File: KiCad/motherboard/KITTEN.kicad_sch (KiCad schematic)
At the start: 40 parts, among them J1 Barrel_Jack_Switch, J10 Conn_01x02_Pin, J2 Conn_01x03_Pin, J3 Conn_01x04_Pin, J4 Conn_01x05_Pin, J5 Conn_01x06_Pin, J6 Conn_01x07_Pin, J7 Conn_01x08_Pin, J8 Conn_01x09_Pin, J9 Conn_01x10_Pin, SW1 Cherry Switch Single, SW10 Cherry Switch Single, SW11 Cherry Switch Single, SW12 Cherry Switch Single, SW13 Cherry Switch Single, SW2 Cherry Switch 1.5x - Enter Key, SW3 Cherry Switch Single, SW4 Cherry Switch Single, SW5 Cherry Switch Single, SW6 Cherry Switch Single, SW7 Cherry Switch Single, SW9 Cherry Switch Single, U2 TMC2209, U3 Display, U4 ICM-20948, U5 24LC512, U6 Adafruit_ICM20948, U7 LTV-817S

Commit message: Work on schematics
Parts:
- removed R1, R10, R11, R2, R3, R4, R5, R6, R7, R8, R9: R, Resistor_SMD:R_0603_1608Metric, symbol Device:R
- removed SW10, SW11, SW12, SW13, SW3, SW4, SW5, SW6, SW7, SW9: Cherry Switch Single, ComponentLib:SW_Cherry_MX_1.00u_PCB, symbol Switch:SW_Push
- removed U4: ICM-20948, ComponentLib:ICM-20948, symbol Sensor_Motion:ICM-20948
- removed U6: Adafruit_ICM20948, ComponentLib:Adafruit-ICM-20948, symbol SymbolLib:Adafruit_ICM20948
- added J11, J12: Conn_01x06_Pin, Connector_JST:JST_PH_B6B-PH-K_1x06_P2.00mm_Vertical, symbol Connector:Conn_01x06_Pin
- added J13: Conn_01x04_Pin, Connector_JST:JST_PH_B4B-PH-K_1x04_P2.00mm_Vertical, symbol Connector:Conn_01x04_Pin
- added U8: TMC2209, ComponentLib:TMC2209 Silentstepstick, symbol SymbolLib:TMC2209_Silentstepstick
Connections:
- net GND: now also J3.4 (Pin_4), J4.4 (Pin_4), J11.2 (Pin_2), J12.2 (Pin_2)
- net +5V: now reaches J3.1 (Pin_1)
- net VREF_measback: now reaches J3.2 (Pin_2)
- net NumpadOut_toADC: now reaches J3.3 (Pin_3)
- net SCL: now reaches J4.1 (Pin_1)
- net SDA: now reaches J4.2 (Pin_2)
- net +3V3: now reaches J4.3 (Pin_3)
- net +3V3: now also J11.1 (Pin_1), J12.1 (Pin_1)
- net ~{RES}: now reaches J4.5 (Pin_5)
- new net CLK: J11.4 (Pin_4), J12.4 (Pin_4)
- new net CS_ENCODER1: J11.3 (Pin_3)
- new net CS_ENCODER2: J12.3 (Pin_3)
- new net MISO: J11.6 (Pin_6), J12.6 (Pin_6)
- new net MOSI: J11.5 (Pin_5), J12.5 (Pin_5)
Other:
- note added: "ICM20948"
- moved on the sheet: J3, J4, U2

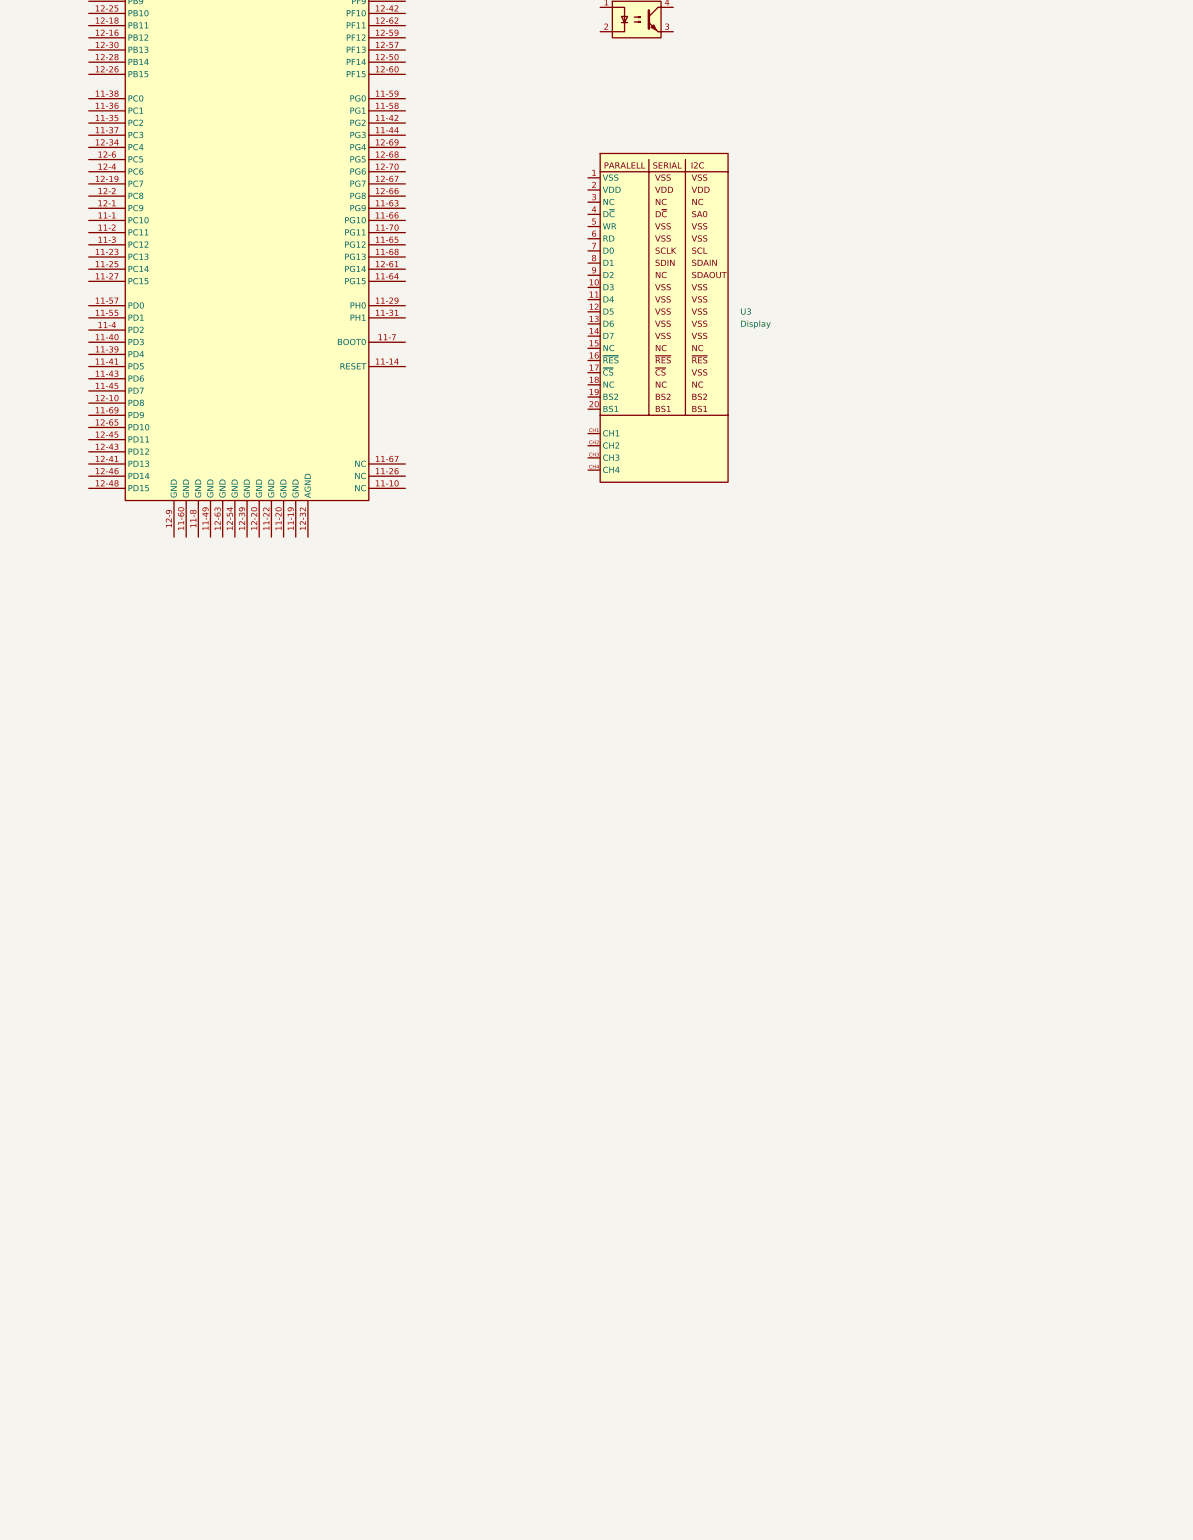
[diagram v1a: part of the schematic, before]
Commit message: Buttons module and main board schematics
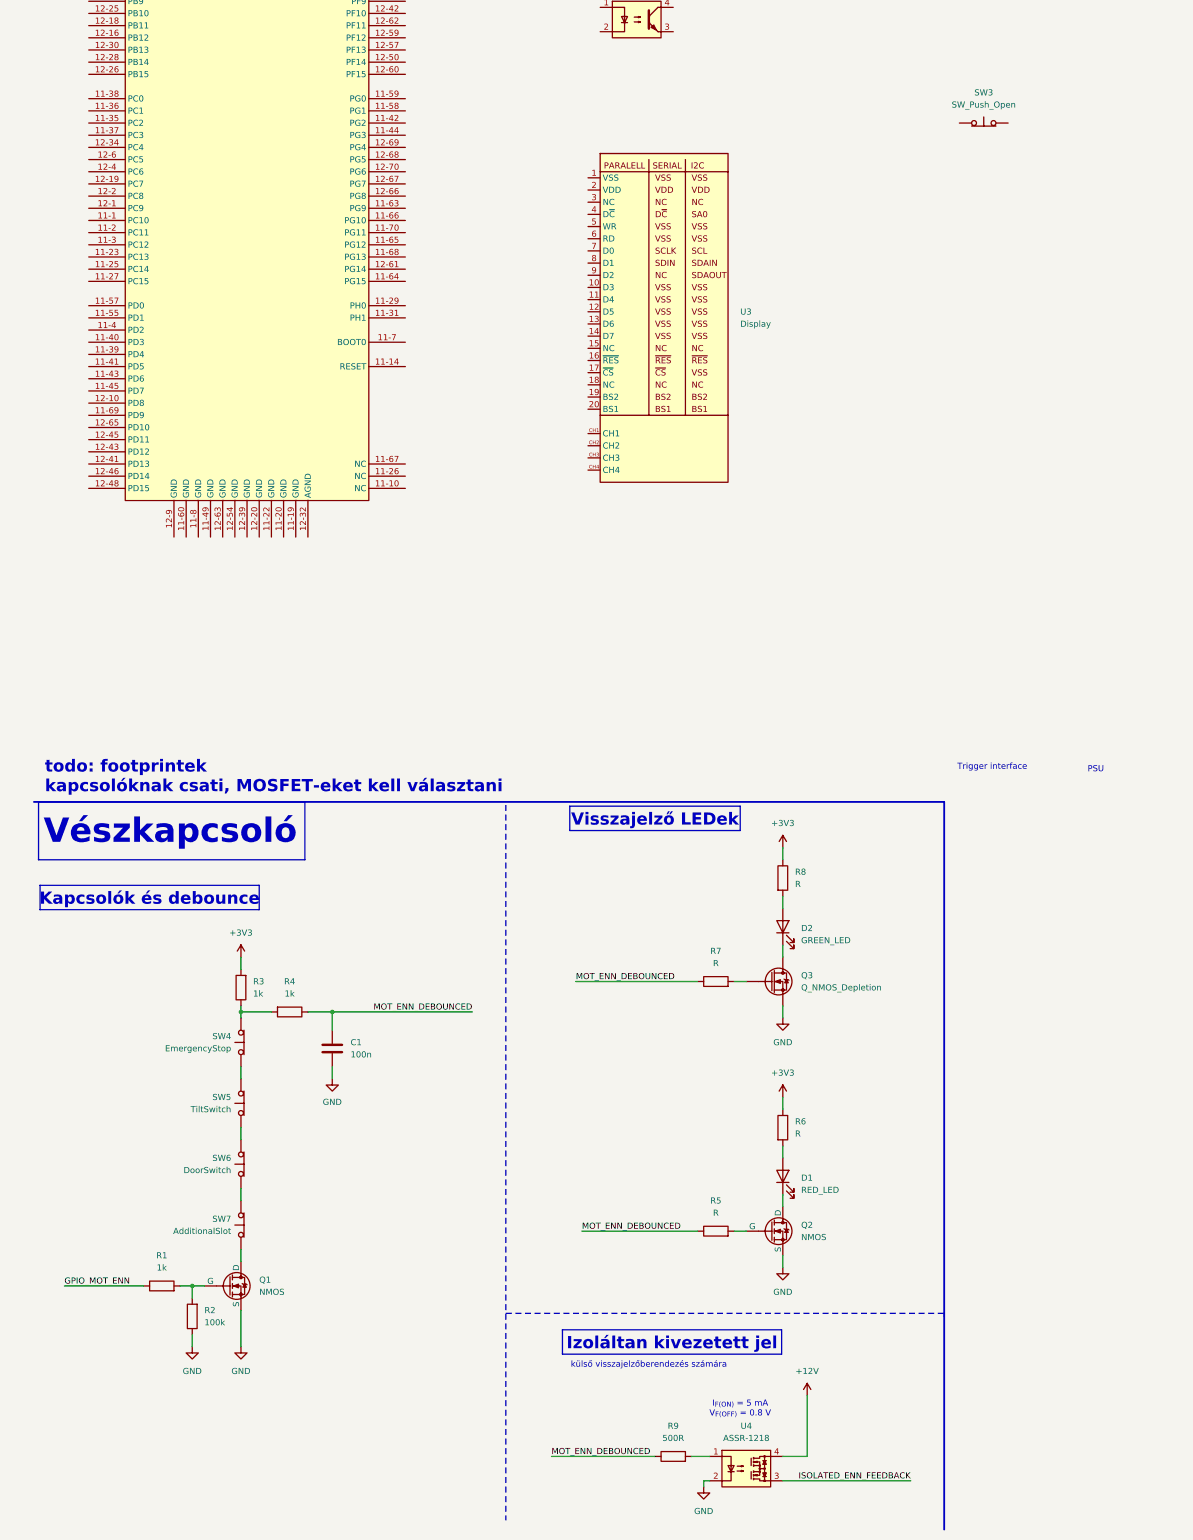
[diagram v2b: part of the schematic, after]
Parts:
- added C1: 100n, symbol Device:C
- added D1: RED_LED, symbol Device:LED
- added D2: GREEN_LED, symbol Device:LED
- added Q1, Q2: NMOS, symbol Simulation_SPICE:NMOS
- added Q3: Q_NMOS_Depletion, symbol Device:Q_NMOS_Depletion
- added R1, R3, R4: 1k, symbol Device:R
- added R2: 100k, symbol Device:R
- added R5, R6, R7, R8: R, symbol Device:R
- added R9: 500R, symbol Device:R
- added SW3: SW_Push_Open, symbol Switch:SW_Push_Open
- added SW4: EmergencyStop, symbol Switch:SW_Push_Open
- added SW5: TiltSwitch, symbol Switch:SW_Push_Open
- added SW6: DoorSwitch, symbol Switch:SW_Push_Open
- added SW7: AdditionalSlot, symbol Switch:SW_Push_Open
- added U4: ASSR-1218, Package_SO:SO-4_4.4x4.3mm_P2.54mm, symbol Relay_SolidState:ASSR-1218
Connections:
- net +3V3: now also R3.2, R6.1, R8.1
- net GND: now also C1.2, Q1.3 (S), Q2.3 (S), Q3.S, R2.1, U4.2
- new net: Q1.2 (G), R1.2, R2.2
- new net: D1.2 (A), R6.2
- new net: D2.1 (K), Q3.D
- new net: D2.2 (A), R8.2
- new net: D1.1 (K), Q2.1 (D)
- new net: Q1.1 (D), SW7.1 (A)
- new net: R3.1, R4.2, SW4.2 (B)
- new net: Q3.G, R7.2
- new net: Q2.2 (G), R5.2
- new net: R9.2, U4.1
- new net: SW6.1 (A), SW7.2 (B)
- new net: SW5.1 (A), SW6.2 (B)
- new net: SW4.1 (A), SW5.2 (B)
- new net +12V: U4.4
- new net GPIO_MOT_ENN: R1.1
- new net ISOLATED_ENN_FEEDBACK: U4.3
- new net MOT_ENN_DEBOUNCED: C1.1, R4.1, R5.1, R7.1, R9.1
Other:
- note added: "I_{F(ON)} = 5 mA V_{F(OFF)} = 0.8 V"
- note added: "Izoláltan kivezetett jel"
- note added: "Kapcsolók és debounce"
- note added: "PSU"
- note added: "Trigger interface"
- note added: "Visszajelző LEDek"
- note added: "Vészkapcsoló"
- note added: "külső visszajelzőberendezés számára"
- note added: "todo: footprintek kapcsolóknak csati, MOSFET-eket kell választani"

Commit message: Main sch further development
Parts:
- removed U3: Display, ComponentLib:NHD-2.23-12832UCB3, symbol SymbolLib:NHD-2.23-12832UCB3
- removed U8: TMC2209, ComponentLib:TMC2209 Silentstepstick, symbol SymbolLib:TMC2209_Silentstepstick
- added C14, C15, C16, C17, C6, C7, C9: 1u, symbol Device:C
- added C18, C19, C20, C21: 100n, Capacitor_SMD:C_0603_1608Metric, symbol Device:C
- added C2, C3, C4, C5: 22u, 35V, symbol Device:C
- added C8: 100n, symbol Device:C
- added D10, D11, D4, D6, D7, D8, D9: GREEN_LED, symbol Device:LED
- added D3: SM15T36CA, Diode_SMD:ST_D_SMC, symbol Diode:SM15T36CA
- added D5: RED_LED, symbol Device:LED
- added F1: Fuse, symbol Device:Fuse
- added J14, J15: Conn_01x04_Pin, Connector_JST:JST_PH_B4B-PH-K_1x04_P2.00mm_Vertical, symbol Connector:Conn_01x04_Pin
- added J16: Conn_01x05_Socket, symbol Connector:Conn_01x05_Socket
- added J17: DB25_Socket_MountingHoles, Connector_Dsub:DSUB-25_Socket_Horizontal_P2.77x2.84mm_EdgePinOffset7.70mm_Housed_MountingHolesOffset9.12mm, symbol Connector:DB25_Socket_MountingHoles
- added J18: Conn_01x09_Pin, Connector_JST:JST_PH_B9B-PH-K_1x09_P2.00mm_Vertical, symbol Connector:Conn_01x09_Pin
- added JP10, JP100, JP101, JP102, JP103, JP104, JP105, JP106, JP107, JP108, JP109, JP11, JP110, JP111, JP112, JP113, JP114, JP115, JP116, JP117, JP118, JP12, JP13, JP14, JP15, JP16, JP17, JP18, JP19, JP20, JP21, JP22, JP23, JP24, JP25, JP26, JP27, JP28, JP29, JP30, JP31, JP32, JP33, JP34, JP35, JP36, JP37, JP38, JP39, JP40, JP41, JP42, JP43, JP44, JP45, JP46, JP47, JP48, JP49, JP50, JP51, JP52, JP53, JP54, JP55, JP56, JP57, JP58, JP59, JP6, JP60, JP61, JP62, JP63, JP64, JP65, JP66, JP67, JP68, JP69, JP7, JP70, JP71, JP72, JP73, JP74, JP75, JP76, JP77, JP78, JP79, JP8, JP80, JP81, JP82, JP83, JP84, JP85, JP86, JP87, JP88, JP89, JP9, JP90, JP91, JP92, JP93, JP94, JP95, JP96, JP97, JP98, JP99: SolderJumper_2_Open, Resistor_SMD:R_0603_1608Metric_Pad0.98x0.95mm_HandSolder, symbol Jumper:SolderJumper_2_Open
- added JP2, JP3, JP4: SolderJumper_2_Open, symbol Jumper:SolderJumper_2_Open
- added Q10, Q5, Q6, Q7, Q8, Q9: BSS138, Package_TO_SOT_SMD:SOT-23, symbol Transistor_FET:BSS138
- added Q4: Si2371EDS, Package_TO_SOT_SMD:SOT-23, symbol Transistor_FET:Si2371EDS
- added R10, R11, R12, R13: R, symbol Device:R
- added R14, R15, R16, R17, R20, R22, R24, R40, R43, R45, R48, R50, R53, R55, R58: 1k, symbol Device:R
- added R18, R21, R27, R28, R29, R30, R42, R47, R52, R57: 100k, symbol Device:R
- added R19, R23, R41, R46, R51, R56: 190R, symbol Device:R
- added R25, R26, R39, R44, R49, R54: 100R, symbol Device:R
- added R59, R61, R63, R65: 1k, Resistor_SMD:R_0603_1608Metric, symbol Device:R
- added R60, R62, R64, R66: 10k, Resistor_SMD:R_0603_1608Metric, symbol Device:R
- added SW12: SW_Push, Connector_PinSocket_2.54mm:PinSocket_1x02_P2.54mm_Vertical, symbol Switch:SW_Push
- added SW13, SW14, SW15: SW_Push, symbol Switch:SW_Push
- added TP1, TP2, TP3, TP4, TP5, TP6: TestPoint, TestPoint:TestPoint_Pad_D2.0mm, symbol Connector:TestPoint
- added TP10, TP11, TP12, TP239, TP240, TP7, TP8, TP9: TestPoint, Connector_PinSocket_2.54mm:PinSocket_1x02_P2.54mm_Vertical, symbol Connector:TestPoint
- added TP100, TP101, TP102, TP103, TP104, TP105, TP106, TP107, TP108, TP109, TP110, TP111, TP112, TP113, TP114, TP115, TP116, TP117, TP118, TP119, TP120, TP121, TP122, TP123, TP124, TP125, TP126, TP127, TP128, TP129, TP13, TP130, TP131, TP132, TP133, TP134, TP135, TP136, TP137, TP138, TP139, TP14, TP140, TP141, TP142, TP143, TP144, TP145, TP146, TP147, TP148, TP149, TP15, TP150, TP151, TP152, TP153, TP154, TP155, TP156, TP157, TP158, TP159, TP16, TP160, TP161, TP162, TP163, TP164, TP165, TP166, TP167, TP168, TP169, TP17, TP170, TP171, TP172, TP173, TP174, TP175, TP176, TP177, TP178, TP179, TP18, TP180, TP181, TP182, TP183, TP184, TP185, TP186, TP187, TP188, TP189, TP19, TP190, TP191, TP192, TP193, TP194, TP195, TP196, TP197, TP198, TP199, TP20, TP200, TP201, TP202, TP203, TP204, TP205, TP206, TP207, TP208, TP209, TP21, TP210, TP211, TP212, TP213, TP214, TP215, TP216, TP217, TP218, TP219, TP22, TP220, TP221, TP222, TP223, TP224, TP225, TP226, TP227, TP228, TP229, TP23, TP230, TP231, TP232, TP233, TP234, TP235, TP236, TP237, TP238, TP24, TP25, TP26, TP27, TP28, TP29, TP30, TP31, TP32, TP33, TP34, TP35, TP36, TP37, TP38, TP39, TP40, TP41, TP42, TP43, TP44, TP45, TP46, TP47, TP48, TP49, TP50, TP51, TP52, TP53, TP54, TP55, TP56, TP57, TP58, TP59, TP60, TP61, TP62, TP63, TP64, TP65, TP66, TP67, TP68, TP69, TP70, TP71, TP72, TP73, TP74, TP75, TP76, TP77, TP78, TP79, TP80, TP81, TP82, TP83, TP84, TP85, TP86, TP87, TP88, TP89, TP90, TP91, TP92, TP93, TP94, TP95, TP96, TP97, TP98, TP99: TestPoint_Small, Connector_PinSocket_2.54mm:PinSocket_1x02_P2.54mm_Vertical, symbol Connector:TestPoint_Small
- added unit 9 of U1
- added unit 6 of U1
- added unit 8 of U1
- added unit 2 of U1
- added unit 4 of U1
- added unit 5 of U1
- added unit 3 of U1
- added unit 7 of U1
- added U10, U11, U12, U13, U14, U8: LTV-817S, Package_DIP:SMDIP-4_W9.53mm, symbol Isolator:LTV-817S
- added U3: TMC2209, ComponentLib:TMC2209 Silentstepstick, symbol SymbolLib:TMC2209_Silentstepstick
- added U6: P7805B-1000, symbol SymbolLib:P78B-1000
- added U9: P7803B-1000, symbol SymbolLib:P78B-1000
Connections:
- net +12V is gone; now on net +5V: U4.4
- net +3V3: now also J13.3 (Pin_3), U2.10 (VIO(3.3-5V)), U5.8 (VCC), C5.1, C8.1, C9.1, D8.2 (A), J18.1 (Pin_1), R28.1, R29.1, R30.1, SW12.2, SW13.2, SW14.2, SW15.2, U10.4, U12.4, U13.4, U14.4, U3.10 (VIO(3.3-5V)), U8.4, U9.3 (VOUT)
- net +5V: now also C14.1, C15.1, C16.1, C17.1, C3.1, C7.1, D7.2 (A), JP118.2 (B), R23.2, R41.2, R46.2, R51.2, R56.2, TP238.1, U6.3 (VOUT)
- net GND: now also J1.2, J1.3, J13.4 (Pin_4), U2.15 (GND), U2.9 (GND), U5.4 (GND), C14.2, C15.2, C16.2, C17.2, C18.2, C19.2, C2.2, C20.2, C21.2, C3.2, C4.2, C5.2, C7.2, C8.2, C9.2, D3.2 (A2), J18.9 (Pin_9), JP2.2 (B), JP3.2 (B), JP4.2 (B), Q6.2 (S), R10.2, R12.2, R13.2, R14.2, R15.2, R21.1, R22.1, R27.2, R40.1, R45.1, R50.1, R55.1, R60.2, R62.2, R64.2, R66.2, U1.11-19 (GND), U1.11-20 (GND), U1.11-22 (GND), U1.11-49 (GND), U1.11-60 (GND), U1.11-8 (GND), U1.12-20 (GND), U1.12-32 (AGND), U1.12-39 (GND), U1.12-54 (GND), U1.12-63 (GND), U1.12-9 (GND), U3.15 (GND), U3.9 (GND), U6.2 (GND), U9.2 (GND)
- net MOT_ENN_DEBOUNCED: now also U2.8 (EN), U3.8 (EN)
- net SCL: now also J13.1 (Pin_1), U5.6 (SCL)
- net SDA: now also J13.2 (Pin_2), U5.5 (SDA)
- net at J1.1: now also F1.1
- net MOT1_DIR: now reaches U2.1 (Dir)
- net at U2.11 (1B): now also J14.1 (Pin_1)
- net at U2.12 (1A): now also J14.2 (Pin_2)
- net at U2.13 (2A): now also J14.3 (Pin_3)
- net at U2.14 (2B): now also J14.4 (Pin_4)
- net +24V: now reaches U2.16 (VM)
- net +24V: now also C2.1, C4.1, D6.2 (A), Q4.2 (S), R11.1, U3.16 (VM), U6.1 (VIN), U9.1 (VIN)
- net MOT1_STEP: now reaches U2.2 (Step)
- net PDN_UART_MOT1: now reaches U2.3 (PDN/UART)
- net PDN_UART_MOT1: now also U2.4 (PDN/UART)
- net MOT1_SPREAD: now reaches U2.5 (SPREAD)
- net MOT1_MS2: now reaches U2.6 (MS2)
- net MOT1_MS1: now reaches U2.7 (MS1)
- net at U5.1 (A0): now also JP2.1 (A), R28.2
- net at U5.2 (A1): now also JP4.1 (A), R30.2
- net at U5.3 (A2): now also JP3.1 (A), R29.2
- net at U5.7 (WP): now also R27.1
- net at U1.11-13 (PA13): now also JP19.1 (A), TP39.1
- net at U1.11-15 (PA14): now also JP20.1 (A), TP41.1
- net at U1.11-17 (PA15): now also JP21.1 (A), TP43.1
- net at U1.11-28 (PA0): now also JP6.1 (A), TP15.1
- net at U1.11-30 (PA1): now also JP7.1 (A), TP14.1
- net at U1.11-32 (PA4): now also JP10.1 (A), TP21.1
- net at U1.12-11 (PA5): now also JP11.1 (A), TP23.1
- net at U1.12-12 (PA12): now also JP18.1 (A), TP37.1
- net at U1.12-13 (PA6): now also JP12.1 (A), TP25.1
- net at U1.12-14 (PA11): now also JP17.1 (A), TP35.1
- net at U1.12-15 (PA7): now also JP13.1 (A), TP27.1
- net at U1.12-21 (PA9): now also JP15.1 (A), TP31.1
- net at U1.12-23 (PA8): now also JP14.1 (A), TP29.1
- net at U1.12-33 (PA10): now also JP16.1 (A), TP33.1
- net at U1.12-35 (PA2): now also JP8.1 (A), TP17.1
- net at U1.12-37 (PA3): now also JP9.1 (A), TP19.1
- new net: R41.1, U8.1
- new net: JP33.2 (B), TP72.1
- new net: JP46.2 (B), TP101.1
- new net: J15.1 (Pin_1), U3.11 (1B)
- new net: J15.2 (Pin_2), U3.12 (1A)
- new net: J15.3 (Pin_3), U3.13 (2A)
- new net: J15.4 (Pin_4), U3.14 (2B)
- new net: JP87.1 (A), TP174.1, U1.11-55 (PD1)
- new net: JP11.2 (B), TP24.1
- new net: JP31.1 (A), TP54.1, U1.12-5 (PB9)
- new net: JP52.1 (A), TP91.1, U1.12-51 (PE14)
- new net: JP52.2 (B), TP107.1
- new net: D11.2 (A), R25.1, U11.3
- new net: JP100.1 (A), TP187.1, U1.12-46 (PD14)
- new net: JP100.2 (B), TP203.1
- new net: JP81.1 (A), TP152.1, U1.11-2 (PC11)
- new net: JP24.1 (A), TP47.1, U1.12-22 (PB2)
- new net: JP24.2 (B), TP63.1
- new net: R51.1, U13.1
- new net: Q9.3 (D), U13.2
- new net: R49.1, R50.2, U13.3
- new net: JP34.1 (A), TP57.1, U1.12-16 (PB12)
- new net: JP72.1 (A), TP143.1, U1.11-35 (PC2)
- new net: D11.1 (K), R24.2
- new net: JP88.1 (A), TP175.1, U1.11-4 (PD2)
- new net: JP73.1 (A), TP144.1, U1.11-37 (PC3)
- new net: JP118.1 (A), TP237.1, U1.11-6 (E5V)
- new net: JP88.2 (B), TP191.1
- new net: JP97.2 (B), TP200.1
- new net: Q7.1 (G), R42.2, R43.1
- new net: JP70.2 (B), TP157.1
- new net: JP60.1 (A), TP115.1, U1.11-9 (PF6)
- new net: JP60.2 (B), TP131.1
- new net: JP80.2 (B), TP167.1
- new net: JP106.2 (B), TP225.1
- new net: JP74.2 (B), TP161.1
- new net: JP94.1 (A), TP181.1, U1.12-10 (PD8)
- new net: Q10.1 (G), R57.2, R58.1
- new net: Q10.3 (D), U14.2
- new net: JP90.1 (A), TP177.1, U1.11-39 (PD4)
- new net: D10.1 (K), R22.2
- new net: JP21.2 (B), TP44.1
- new net: JP85.1 (A), TP156.1, U1.11-27 (PC15)
- new net: JP115.1 (A), TP218.1, U1.11-68 (PG13)
- new net: JP8.2 (B), TP18.1
- new net: JP50.2 (B), TP105.1
- new net: JP103.1 (A), TP206.1, U1.11-58 (PG1)
- new net: JP105.1 (A), TP208.1, U1.11-44 (PG3)
- new net: JP105.2 (B), TP224.1
- new net: JP53.2 (B), TP108.1
- new net: JP113.2 (B), TP232.1
- new net: JP25.2 (B), TP64.1
- new net: JP48.2 (B), TP103.1
- new net: JP84.1 (A), TP155.1, U1.11-25 (PC14)
- new net: JP84.2 (B), TP171.1
- new net: JP92.1 (A), TP179.1, U1.11-43 (PD6)
- new net: JP38.2 (B), TP93.1
- new net: JP99.1 (A), TP186.1, U1.12-41 (PD13)
- new net: Q9.1 (G), R52.2, R53.1
- new net: JP63.2 (B), TP134.1
- new net: JP33.1 (A), TP56.1, U1.12-18 (PB11)
- new net: Q8.1 (G), R47.2, R48.1
- new net: JP61.1 (A), TP116.1, U1.11-11 (PF7)
- new net: JP47.1 (A), TP86.1, U1.12-52 (PE9)
- new net: JP10.2 (B), TP22.1
- new net: JP85.2 (B), TP172.1
- new net: JP39.2 (B), TP94.1
- new net: JP14.2 (B), TP30.1
- new net: JP61.2 (B), TP132.1
- new net: JP23.2 (B), TP62.1
- new net: JP109.1 (A), TP212.1, U1.12-67 (PG7)
- new net: JP109.2 (B), TP228.1
- new net: R59.1, SW12.1
- new net: JP51.2 (B), TP106.1
- new net: JP116.1 (A), TP219.1, U1.12-61 (PG14)
- new net: JP116.2 (B), TP235.1
- new net: JP56.1 (A), TP111.1, U1.11-52 (PF2)
- new net: JP15.2 (B), TP32.1
- new net: JP29.2 (B), TP68.1
- new net: JP25.1 (A), TP48.1, U1.12-31 (PB3)
- new net: JP36.1 (A), TP59.1, U1.12-28 (PB14)
- new net: JP36.2 (B), TP75.1
- new net: R46.1, U12.1
- new net: Q8.3 (D), U12.2
- new net: R44.1, R45.2, U12.3
- new net: JP35.2 (B), TP74.1
- new net: JP104.1 (A), TP207.1, U1.11-42 (PG2)
- new net: JP79.1 (A), TP150.1, U1.12-1 (PC9)
- new net: JP58.1 (A), TP113.1, U1.12-38 (PF4)
- new net: JP102.1 (A), TP205.1, U1.11-59 (PG0)
- new net: JP102.2 (B), TP221.1
- new net: JP67.1 (A), TP122.1, U1.12-57 (PF13)
- new net: JP67.2 (B), TP138.1
- new net: JP43.2 (B), TP98.1
- new net: JP106.1 (A), TP209.1, U1.12-69 (PG4)
- new net: JP104.2 (B), TP223.1
- new net: JP59.2 (B), TP130.1
- new net: JP55.1 (A), TP110.1, U1.11-51 (PF1)
- new net: JP54.1 (A), TP109.1, U1.11-53 (PF0)
- new net: JP62.1 (A), TP117.1, U1.11-54 (PF8)
- new net: JP63.1 (A), TP118.1, U1.11-56 (PF9)
- new net: JP59.1 (A), TP114.1, U1.12-36 (PF5)
- new net: JP64.1 (A), TP119.1, U1.12-42 (PF10)
- new net: JP68.1 (A), TP123.1, U1.12-50 (PF14)
- new net: JP57.1 (A), TP112.1, U1.12-58 (PF3)
- new net: JP66.1 (A), TP121.1, U1.12-59 (PF12)
- new net: JP69.1 (A), TP124.1, U1.12-60 (PF15)
- new net: JP65.1 (A), TP120.1, U1.12-62 (PF11)
- new net: JP93.2 (B), TP196.1
- new net: JP74.1 (A), TP145.1, U1.12-34 (PC4)
- new net: JP98.1 (A), TP185.1, U1.12-43 (PD12)
- new net: JP48.1 (A), TP87.1, U1.12-47 (PE10)
- new net: JP38.1 (A), TP77.1, U1.12-64 (PE0)
- new net: JP75.1 (A), TP146.1, U1.12-6 (PC5)
- new net: JP73.2 (B), TP160.1
- new net: Q7.3 (D), U8.2
- new net: R39.1, R40.2, U8.3
- new net: R19.1, U10.1
- new net: JP39.1 (A), TP78.1, U1.11-61 (PE1)
- new net: JP30.1 (A), TP53.1, U1.12-3 (PB8)
- new net: JP79.2 (B), TP166.1
- new net: JP94.2 (B), TP197.1
- new net: D3.1 (A1), D4.2 (A), D5.1 (K), F1.2, Q4.3 (D)
- new net: JP115.2 (B), TP234.1
- new net: JP96.1 (A), TP183.1, U1.12-65 (PD10)
- new net: D6.1 (K), R13.1
- new net: JP28.2 (B), TP67.1
- new net: JP114.1 (A), TP217.1, U1.11-65 (PG12)
- new net: JP103.2 (B), TP222.1
- new net: R63.1, SW14.1
- new net: JP51.1 (A), TP90.1, U1.12-55 (PE13)
- new net: JP87.2 (B), TP190.1
- new net: JP44.2 (B), TP99.1
- new net: JP16.2 (B), TP34.1
- new net: JP98.2 (B), TP201.1
- new net: Q5.1 (G), R17.1, R18.2
- new net: JP37.1 (A), TP60.1, U1.12-26 (PB15)
- new net: JP37.2 (B), TP76.1
- new net: JP62.2 (B), TP133.1
- new net: JP28.1 (A), TP51.1, U1.12-17 (PB6)
- new net: JP27.1 (A), TP50.1, U1.12-29 (PB5)
- new net: JP27.2 (B), TP66.1
- new net: JP31.2 (B), TP70.1
- new net: JP99.2 (B), TP202.1
- new net: D9.1 (K), R16.2
- new net: JP111.1 (A), TP214.1, U1.11-63 (PG9)
- new net: JP111.2 (B), TP230.1
- new net: JP55.2 (B), TP126.1
- new net: JP50.1 (A), TP89.1, U1.12-49 (PE12)
- new net: JP101.1 (A), TP188.1, U1.12-48 (PD15)
- new net: JP101.2 (B), TP204.1
- new net: JP108.1 (A), TP211.1, U1.12-70 (PG6)
- new net: JP108.2 (B), TP227.1
- new net: JP92.2 (B), TP195.1
- new net: JP80.1 (A), TP151.1, U1.11-1 (PC10)
- new net: JP29.1 (A), TP52.1, U1.11-21 (PB7)
- new net: JP22.1 (A), TP45.1, U1.11-34 (PB0)
- new net: JP23.1 (A), TP46.1, U1.12-24 (PB1)
- new net: JP32.1 (A), TP55.1, U1.12-25 (PB10)
- new net: JP26.1 (A), TP49.1, U1.12-27 (PB4)
- new net: JP35.1 (A), TP58.1, U1.12-30 (PB13)
- new net: JP86.1 (A), TP173.1, U1.11-57 (PD0)
- new net: JP86.2 (B), TP189.1
- new net: JP113.1 (A), TP216.1, U1.11-70 (PG11)
- new net: JP49.1 (A), TP88.1, U1.12-56 (PE11)
- new net: JP49.2 (B), TP104.1
- new net: JP32.2 (B), TP71.1
- new net: JP19.2 (B), TP40.1
- new net: JP78.1 (A), TP149.1, U1.12-2 (PC8)
- new net: JP69.2 (B), TP140.1
- new net: JP6.2 (B), TP13.1
- new net: JP42.1 (A), TP81.1, U1.11-48 (PE4)
- new net: JP20.2 (B), TP42.1
- new net: JP76.2 (B), TP163.1
- new net: JP90.2 (B), TP193.1
- new net: JP66.2 (B), TP137.1
- new net: JP89.1 (A), TP176.1, U1.11-40 (PD3)
- new net: JP91.1 (A), TP178.1, U1.11-41 (PD5)
- new net: JP93.1 (A), TP180.1, U1.11-45 (PD7)
- new net: JP95.1 (A), TP182.1, U1.11-69 (PD9)
- new net: JP97.1 (A), TP184.1, U1.12-45 (PD11)
- new net: JP91.2 (B), TP194.1
- new net: JP65.2 (B), TP136.1
- new net: JP64.2 (B), TP135.1
- new net: JP71.1 (A), TP142.1, U1.11-36 (PC1)
- new net: JP40.1 (A), TP79.1, U1.11-46 (PE2)
- new net: JP41.1 (A), TP80.1, U1.11-47 (PE3)
- new net: JP43.1 (A), TP82.1, U1.11-50 (PE5)
- new net: JP44.1 (A), TP83.1, U1.11-62 (PE6)
- new net: JP46.1 (A), TP85.1, U1.12-40 (PE8)
- new net: JP45.1 (A), TP84.1, U1.12-44 (PE7)
- new net: JP53.1 (A), TP92.1, U1.12-53 (PE15)
- new net: R65.1, SW15.1
- new net: JP12.2 (B), TP26.1
- new net: Q6.1 (G), R20.1, R21.2
- new net: Q6.3 (D), U11.2
- new net: JP112.2 (B), TP231.1
- new net: JP82.1 (A), TP153.1, U1.11-3 (PC12)
- new net: JP42.2 (B), TP97.1
- new net: JP75.2 (B), TP162.1
- new net: JP114.2 (B), TP233.1
- new net: JP70.1 (A), TP141.1, U1.11-38 (PC0)
- new net: JP96.2 (B), TP199.1
- new net: D10.2 (A), R26.2, U10.3
- new net: JP77.2 (B), TP164.1
- new net: JP57.2 (B), TP128.1
- new net: JP13.2 (B), TP28.1
- new net: JP78.2 (B), TP165.1
- new net: JP17.2 (B), TP36.1
- new net: JP76.1 (A), TP147.1, U1.12-4 (PC6)
- new net: JP45.2 (B), TP100.1
- new net: JP112.1 (A), TP215.1, U1.11-66 (PG10)
- new net: JP34.2 (B), TP73.1
- new net: JP22.2 (B), TP61.1
- new net: R23.1, U11.1
- new net: JP30.2 (B), TP69.1
- new net: JP83.1 (A), TP154.1, U1.11-23 (PC13)
- new net: JP83.2 (B), TP170.1
- new net: D8.1 (K), R15.1
- new net: JP40.2 (B), TP95.1
- new net: JP47.2 (B), TP102.1
- new net: JP77.1 (A), TP148.1, U1.12-19 (PC7)
- new net: JP56.2 (B), TP127.1
- new net: JP71.2 (B), TP158.1
- new net: JP81.2 (B), TP168.1
- new net: JP95.2 (B), TP198.1
- new net: JP89.2 (B), TP192.1
- new net: JP82.2 (B), TP169.1
- new net: JP54.2 (B), TP125.1
- new net: JP7.2 (B), TP16.1
- new net: JP117.1 (A), TP220.1, U1.11-64 (PG15)
- new net: JP117.2 (B), TP236.1
- new net: JP41.2 (B), TP96.1
- new net: JP107.2 (B), TP226.1
- new net: JP107.1 (A), TP210.1, U1.12-68 (PG5)
- new net: JP110.1 (A), TP213.1, U1.12-66 (PG8)
- new net: Q4.1 (G), R11.2, R12.1
- new net: JP68.2 (B), TP139.1
- new net: D4.1 (K), D5.2 (A), R10.1
- new net: JP9.2 (B), TP20.1
- new net: JP26.2 (B), TP65.1
- new net: R54.1, R55.2, U14.3
- new net: D7.1 (K), R14.1
- new net: JP18.2 (B), TP38.1
- new net: JP58.2 (B), TP129.1
- new net: R56.1, U14.1
- new net: Q5.3 (D), U10.2
- new net: JP72.2 (B), TP159.1
- new net: JP110.2 (B), TP229.1
- new net: R61.1, SW13.1
- new net BTN_ADDITIONAL: J18.8 (Pin_8)
- new net BTN_FIX_AX: J18.2 (Pin_2)
- new net BTN_FREE_MOOVE: J18.7 (Pin_7)
- new net BTN_MEMSLOT: J18.4 (Pin_4)
- new net BTN_OK: J18.5 (Pin_5)
- new net BTN_SET: J18.6 (Pin_6)
- new net BTN_TRACKED_AX: J18.3 (Pin_3)
- new net CLK_LISTEN: R49.2, TP11.1
- new net CLK_LISTEN_EXTERNAL: J16.3 (Pin_3), R53.2, TP12.1
- new net EXTRA_BTN_1: C18.1, R59.2, R60.1
- new net EXTRA_BTN_2: C19.1, R61.2, R62.1
- new net EXTRA_BTN_3: C20.1, R63.2, R64.1
- new net EXTRA_BTN_4: C21.1, R65.2, R66.1
- new net GND_SPI_LISTEN: J16.5 (Pin_5), Q10.2 (S), Q7.2 (S), Q8.2 (S), Q9.2 (S), R42.1, R47.1, R52.1, R57.1
- new net GND_TRG: C6.2, J17.0 (PAD), J17.24 (P24), J17.25 (P25), J17.5, Q5.2 (S), R16.1, R18.1, R24.1, TP6.1
- new net MISO_LISTEN: R44.2, TP9.1
- new net MISO_LISTEN_EXTERNAL: J16.2 (Pin_2), R48.2, TP7.1
- new net MOSI_LISTEN: R39.2, TP10.1
- new net MOSI_LISTEN_EXTERNAL: J16.1 (Pin_1), R43.2, TP8.1
- new net MOT2_DIR: U3.1 (Dir)
- new net MOT2_MS1: U3.7 (MS1)
- new net MOT2_MS2: U3.6 (MS2)
- new net MOT2_SPREAD: U3.5 (SPREAD)
- new net MOT2_STEP: U3.2 (Step)
- new net NSS_LISTEN: R54.2, TP239.1
- new net NSS_LISTEN_EXTERNAL: J16.4 (Pin_4), R58.2, TP240.1
- new net PDN_UART_MOT2: U3.3 (PDN/UART), U3.4 (PDN/UART)
- new net SIMU_TRG_RB: J17.1, R25.2, TP1.1
- new net SIMU_TRG_SIGNAL: J17.12, R17.2, TP4.1
- new net TRG_RB_SIGNAL: R20.2, TP2.1
- new net TRG_SIGNAL: R26.1, TP3.1
- new net VCC_TRG: C6.1, D9.2 (A), J17.18 (P18), R19.2, TP5.1, U11.4
- no-connect marks 0 -> 6
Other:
- note added: "100R miért? Csak, h ne közvetlenül menjen?"
- note added: "Csatlakozó"
- note added: "DC-DC 3V3"
- note added: "DC-DC 5V"
- note added: "EEPROM"
- note added: "ENCODER 1"
- note added: "ESD"
- note added: "Ez csak placeholder, meg kell beszélni a típusát még"
- note added: "Ez nem tudom, jó választás-e. Azért ez van itt, mert ez már bennt volt a könyvtárnam, kétiránú és VRM = 30.8V"
- note added: "Ez így miért nem jó, hogy nem 5V és 3v3 zener, hanem simán a 3v3-at kapcsolom"
- note added: "GOMBOK"
- note added: "I_{C max} = 30 ma"
- note added: "MCU"
- note added: "MODULOK"
- note added: "Minden lábnál így"
- note added: "Motorvezérlők"
- note added: "NUMPAD"
- note added: "OELD"
- note added: "Polarity indication"
- note added: "Polarity indication?"
- note added: "Pull downt azért raktam, mert le van választva -> nincs aktívan hajtva az alacsony szint Nem terheli ezn agyon a lehallgatottat? Milyen csati kellene?"
- note added: "REF SZENZOR"
- note added: "SIMU"
- note added: "SPI SNIFFER"
- note added: "Simulizer -> MCU trigger jel izoláció"
- note added: "Simulizer <- MCU trigger jel izoláció"
- note added: "TOVÁBBI GOMBOK ELŐKÉSZÍTÉSE"
- note added: "Táp"
- note added: "V_{F} = 1.2V I_{F} = 20mA"
- note removed: "ICM20948"
- note removed: "PSU"
- moved on the sheet: J1, J10, J11, J12, J13, J2, J3, J4, J5, J6, J7, J8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

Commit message: MAIN board schematic mostly done
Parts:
- removed J10: Conn_01x02_Pin, Connector_JST:JST_PH_B2B-PH-K_1x02_P2.00mm_Vertical, symbol Connector:Conn_01x02_Pin
- removed J2: Conn_01x03_Pin, Connector_JST:JST_PH_B3B-PH-K_1x03_P2.00mm_Vertical, symbol Connector:Conn_01x03_Pin
- removed J5: Conn_01x06_Pin, Connector_JST:JST_PH_B6B-PH-K_1x06_P2.00mm_Vertical, symbol Connector:Conn_01x06_Pin
- removed J6: Conn_01x07_Pin, Connector_JST:JST_PH_B7B-PH-K_1x07_P2.00mm_Vertical, symbol Connector:Conn_01x07_Pin
- removed J7: Conn_01x08_Pin, Connector_JST:JST_PH_B8B-PH-K_1x08_P2.00mm_Vertical, symbol Connector:Conn_01x08_Pin
- removed J8: Conn_01x09_Pin, Connector_JST:JST_PH_B9B-PH-K_1x09_P2.00mm_Vertical, symbol Connector:Conn_01x09_Pin
- removed J9: Conn_01x10_Pin, Connector_JST:JST_PH_B10B-PH-K_1x10_P2.00mm_Vertical, symbol Connector:Conn_01x10_Pin
- removed SW1: Cherry Switch Single, ComponentLib:SW_Cherry_MX_1.00u_PCB, symbol Switch:SW_Push
- removed SW2: Cherry Switch 1.5x - Enter Key, ComponentLib:SW_Cherry_MX_1.50u_PCB, symbol Switch:SW_Push
- removed SW3: SW_Push_Open, symbol Switch:SW_Push_Open
- removed U7: LTV-817S, Package_DIP:SMDIP-4_W9.53mm, symbol Isolator:LTV-817S
- added R31, R32: R, symbol Device:R
- added TP241, TP242: TestPoint, Connector_PinSocket_2.54mm:PinSocket_1x02_P2.54mm_Vertical, symbol Connector:TestPoint
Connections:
- net BTN_ADDITIONAL is gone; now on net BTN_EXTERNAL_EXTRA: J18.8 (Pin_8)
- net CLK is gone; now on net SPI_SCK: J11.4 (Pin_4), J12.4 (Pin_4)
- net EXTRA_BTN_1 is gone; now on net BTN_ONBRD_EXTRA1: C18.1, R59.2, R60.1
- net EXTRA_BTN_2 is gone; now on net BTN_ONBRD_EXTRA2: C19.1, R61.2, R62.1
- net EXTRA_BTN_3 is gone; now on net BTN_ONBRD_EXTRA3: C20.1, R63.2, R64.1
- net EXTRA_BTN_4 is gone; now on net BTN_ONBRD_EXTRA4: C21.1, R65.2, R66.1
- net MISO is gone; now on net SPI_MISO: J11.6 (Pin_6), J12.6 (Pin_6)
- net MOSI is gone; now on net SPI_MOSI: J11.5 (Pin_5), J12.5 (Pin_5)
- net NumpadOut_toADC is gone; now on net NUMPAD_A_OUT: J3.3 (Pin_3)
- net SCL is gone; now on net I2C_SCL: J13.1 (Pin_1), J4.1 (Pin_1), U5.6 (SCL)
- net SDA is gone; now on net I2C_SDA: J13.2 (Pin_2), J4.2 (Pin_2), U5.5 (SDA)
- net TRG_RB_SIGNAL is gone; now on net TRG_RB_OUT: R20.2, TP2.1
- net VREF_measback is gone; now on net NUMPAD_VREF: J3.2 (Pin_2)
- net ~{RES} is gone; now on net OLED_~{RES}: J4.5 (Pin_5)
- net +3V3: now also R31.1, R32.1
- net BTN_FIX_AX: now also JP40.2 (B), TP95.1
- net BTN_FREE_MOOVE: now also JP45.2 (B), TP100.1
- net BTN_MEMSLOT: now also JP42.2 (B), TP97.1
- net BTN_OK: now also JP43.2 (B), TP98.1
- net BTN_SET: now also JP44.2 (B), TP99.1
- net BTN_TRACKED_AX: now also JP41.2 (B), TP96.1
- net CLK_LISTEN: now also JP32.2 (B), JP80.2 (B), TP167.1, TP71.1
- net CS_ENCODER1: now also JP64.2 (B), TP135.1
- net CS_ENCODER2: now also JP65.2 (B), TP136.1
- net GPIO_MOT_ENN: now also JP62.2 (B), TP133.1
- net MISO_LISTEN: now also JP24.2 (B), TP63.1
- net MOSI_LISTEN: now also JP73.2 (B), TP160.1
- net MOT1_DIR: now also JP54.2 (B), TP125.1
- net MOT1_MS1: now also JP56.2 (B), TP127.1
- net MOT1_MS2: now also JP57.2 (B), TP128.1
- net MOT1_SPREAD: now also JP55.2 (B), TP126.1
- net MOT1_STEP: now also JP6.2 (B), TP13.1
- net MOT2_DIR: now also JP58.2 (B), TP129.1
- net MOT2_MS1: now also JP60.2 (B), TP131.1
- net MOT2_MS2: now also JP61.2 (B), TP132.1
- net MOT2_SPREAD: now also JP59.2 (B), TP130.1
- net MOT2_STEP: now also JP21.2 (B), TP44.1
- net MOT_ENN_DEBOUNCED: now also JP38.2 (B), TP93.1
- net NSS_LISTEN: now also JP10.2 (B), JP34.2 (B), TP22.1, TP73.1
- net PDN_UART_MOT1: now also JP82.2 (B), TP169.1
- net PDN_UART_MOT2: now also JP87.2 (B), TP190.1
- net TRG_SIGNAL: now also JP39.2 (B), TP94.1
- net BTN_EXTERNAL_EXTRA: now reaches JP46.2 (B), TP101.1
- net MOT2_DIAG: now reaches U3.17 (DIAG)
- net MOT2_DIAG: now also JP52.2 (B), TP107.1
- net MOT2_INDEX: now reaches U3.18 (INDEX)
- net MOT2_INDEX: now also TP241.1
- net SPI_SCK: now reaches JP11.2 (B), TP24.1
- net BTN_ONBRD_EXTRA4: now reaches JP50.2 (B), TP105.1
- net BTN_ONBRD_EXTRA2: now reaches JP48.2 (B), TP103.1
- net OLED_~{RES}: now reaches JP63.2 (B), TP134.1
- net MOT1_DIAG: now reaches JP51.2 (B), TP106.1
- net MOT1_DIAG: now also U2.17 (DIAG)
- net SPI_MOSI: now reaches JP27.2 (B), TP66.1
- net I2C_SDA: now reaches JP31.2 (B), TP70.1
- net I2C_SDA: now also R32.2
- net SPI_MISO: now reaches JP111.2 (B), TP230.1
- net BTN_ONBRD_EXTRA3: now reaches JP49.2 (B), TP104.1
- net TRG_RB_OUT: now reaches JP66.2 (B), TP137.1
- net NUMPAD_VREF: now reaches JP12.2 (B), TP26.1
- net I2C_SCL: now reaches JP30.2 (B), TP69.1
- net I2C_SCL: now also R31.2
- net MOT1_INDEX: now reaches U2.18 (INDEX)
- net MOT1_INDEX: now also TP242.1
- net BTN_ONBRD_EXTRA1: now reaches JP47.2 (B), TP102.1
- net NUMPAD_A_OUT: now reaches JP9.2 (B), TP20.1
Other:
- note removed: "Minden lábnál így"
- moved on the sheet: C14, C15, C16, C17, J16, JP10, JP100, JP101, JP102, JP103, JP104, JP105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
